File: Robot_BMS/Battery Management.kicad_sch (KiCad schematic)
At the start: 33 parts, among them IC2 BQ76922RSNR, Q4 SIS413DN-T1-GE3, Q5 2N7002, Q6 SIS413DN-T1-GE3

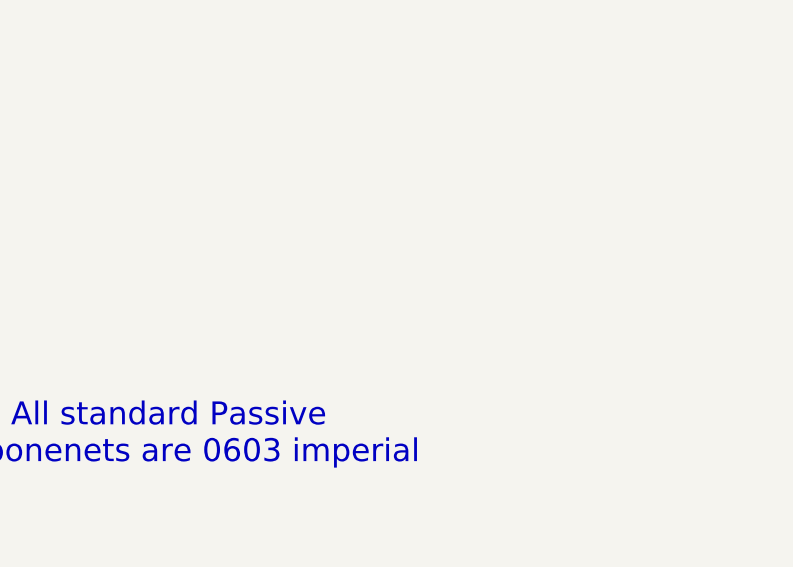
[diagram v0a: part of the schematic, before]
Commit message: adding qwik connectors replacing old jst ph 6 pin ones
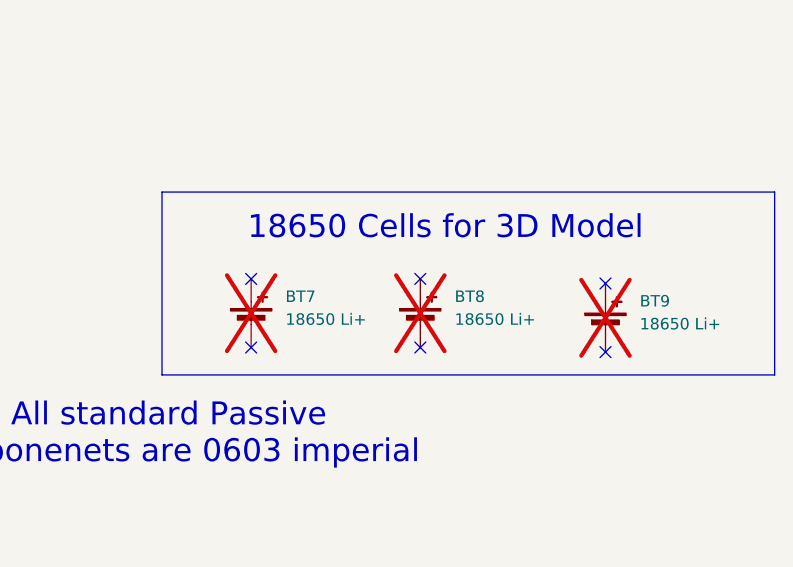
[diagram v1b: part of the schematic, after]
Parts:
- added BT7, BT8, BT9: 18650 Li+, RobotBMS:18650 Battery, symbol Device:Battery_Cell
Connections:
- no-connect marks 6 -> 12
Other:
- note added: "18650 Cells for 3D Model"
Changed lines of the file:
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@@
 	)
 	(no_connect
+		(at 226.06 162.814)
+	)
+	(no_connect
+		(at 265.43 155.702)
+	)
+	(no_connect
 		(at 130.048 122.936)
 	)
 	(no_connect
+		(at 265.43 163.322)
+	)
+	(no_connect
 		(at 127.508 122.936)
 	)
 	(no_connect
+		(at 244.856 162.814)
+	)
+	(no_connect
+		(at 226.06 155.194)
+	)
+	(no_connect
+		(at 244.856 155.194)
+	)
+	(no_connect
 		(at 145.288 94.996)
 	)
@@
 		)
 	)
+	(rectangle
+		(start 216.154 145.542)
+		(end 284.226 165.862)
+		(stroke
+			(width 0)
+			(type default)
+		)
+		(fill
+			(type none)
+		)
+	)
 	(text "Wires highlighted\nto avoid confusion\ndue to crossovers"
 		(exclude_from_sim no)
@@
 		)
 	)
+	(text "18650 Cells for 3D Model\n"
+		(exclude_from_sim no)
+		(at 247.65 149.606 0)
+		(effects
+			(font
+				(size 2.54 2.54)
+			)
+		)
+	)
 	(text "10A Resettable fuse\n\n"
 		(exclude_from_sim no)
@@
 	)
 	(symbol
+		(lib_id "Device:Battery_Cell")
+		(at 226.06 160.274 0)
+		(unit 1)
+		(exclude_from_sim no)
+		(in_bom no)
+		(on_board yes)
+		(dnp yes)
+		(fields_autoplaced yes)
+		(property "Reference" "BT7"
+			(at 229.87 157.1624 0)
+			(effects
+				(font
+					(size 1.27 1.27)
+				)
+				(justify left)
+			)
+		)
+		(property "Value" "18650 Li+"
+			(at 229.87 159.7024 0)
+			(effects
+				(font
+					(size 1.27 1.27)
+				)
+				(justify left)
+			)
+		)
+		(property "Footprint" "RobotBMS:18650 Battery"
+			(at 226.06 158.75 90)
+			(effects
+				(font
+					(size 1.27 1.27)
+				)
+				(hide yes)
+			)
+		)
+		(property "Datasheet" "~"
+			(at 226.06 158.75 90)
+			(effects
+				(font
+					(size 1.27 1.27)
+				)
+				(hide yes)
+			)
+		)
+		(property "Description" "Single-cell battery"
+			(at 226.06 160.274 0)
+			(effects
+				(font
+					(size 1.27 1.27)
+				)
+				(hide yes)
+			)
+		)
+		(pin "1"
+		)
+		(pin "2"
+		)
+		(instances
+			(project ""
+				(path "/72551b1c-3d40-4199-8911-e5b015f4abec/26a1c9c5-a214-45fb-a345-5a76cfe84f03"
+					(reference "BT7")
+					(unit 1)
+				)
+			)
+		)
+	)
+	(symbol
 		(lib_name "BK-18650-CLIP_1")
 		(lib_id "BK-18650-Clip:BK-18650-CLIP")
@@
 	)
 	(symbol
+		(lib_id "Device:Battery_Cell")
+		(at 265.43 160.782 0)
+		(unit 1)
+		(exclude_from_sim no)
+		(in_bom no)
+		(on_board yes)
+		(dnp yes)
+		(fields_autoplaced yes)
+		(property "Reference" "BT9"
+			(at 269.24 157.6704 0)
+			(effects
+				(font
+					(size 1.27 1.27)
+				)
+				(justify left)
+			)
+		)
+		(property "Value" "18650 Li+"
+			(at 269.24 160.2104 0)
+			(effects
+				(font
+					(size 1.27 1.27)
+				)
+				(justify left)
+			)
+		)
+		(property "Footprint" "RobotBMS:18650 Battery"
+			(at 265.43 159.258 90)
+			(effects
+				(font
+					(size 1.27 1.27)
+				)
+				(hide yes)
+			)
+		)
+		(property "Datasheet" "~"
+			(at 265.43 159.258 90)
+			(effects
+				(font
+					(size 1.27 1.27)
+				)
+				(hide yes)
+			)
+		)
+		(property "Description" "Single-cell battery"
+			(at 265.43 160.782 0)
+			(effects
+				(font
+					(size 1.27 1.27)
+				)
+				(hide yes)
+			)
+		)
+		(pin "1"
+		)
+		(pin "2"
+		)
+		(instances
+			(project "Robot_BMS"
+				(path "/72551b1c-3d40-4199-8911-e5b015f4abec/26a1c9c5-a214-45fb-a345-5a76cfe84f03"
+					(reference "BT9")
+					(unit 1)
+				)
+			)
+		)
+	)
+	(symbol
 		(lib_name "BK-18650-CLIP_1")
 		(lib_id "BK-18650-Clip:BK-18650-CLIP")
@@
 					(unit 1)
 				)
+			)
+		)
+	)
+	(symbol
+		(lib_id "Device:Battery_Cell")
+		(at 244.856 160.274 0)
+		(unit 1)
+		(exclude_from_sim no)
+		(in_bom no)
+		(on_board yes)
+		(dnp yes)
+		(fields_autoplaced yes)
+		(property "Reference" "BT8"
+			(at 248.666 157.1624 0)
+			(effects
+				(font
+					(size 1.27 1.27)
+				)
+				(justify left)
+			)
+		)
+		(property "Value" "18650 Li+"
+			(at 248.666 159.7024 0)
+			(effects
+				(font
+					(size 1.27 1.27)
+				)
+				(justify left)
+			)
+		)
+		(property "Footprint" "RobotBMS:18650 Battery"
+			(at 244.856 158.75 90)
+			(effects
+				(font
+					(size 1.27 1.27)
+				)
+				(hide yes)
+			)
+		)
+		(property "Datasheet" "~"
+			(at 244.856 158.75 90)
+			(effects
+				(font
+					(size 1.27 1.27)
+				)
+				(hide yes)
+			)
+		)
+		(property "Description" "Single-cell battery"
+			(at 244.856 160.274 0)
+			(effects
+				(font
+					(size 1.27 1.27)
+				)
+				(hide yes)
+			)
+		)
+		(pin "1"
+		)
+		(pin "2"
+		)
+		(instances
+			(project "Robot_BMS"
+				(path "/72551b1c-3d40-4199-8911-e5b015f4abec/26a1c9c5-a214-45fb-a345-5a76cfe84f03"
+					(reference "BT8")
+					(unit 1)
+				)

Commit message: creation of seperate 4 layer pcb for individual technical report
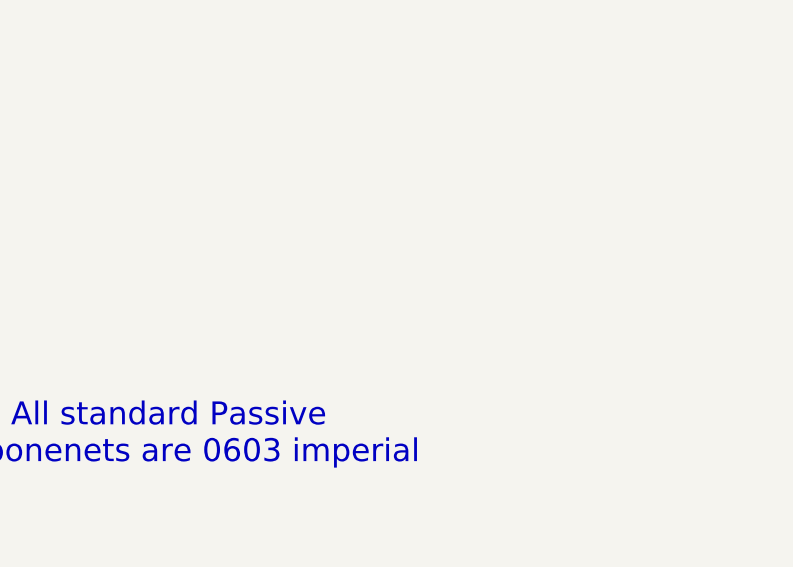
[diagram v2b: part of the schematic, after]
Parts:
- removed BT7, BT8, BT9: 18650 Li+, RobotBMS:18650 Battery, symbol Device:Battery_Cell
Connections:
- no-connect marks 12 -> 6
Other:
- note removed: "18650 Cells for 3D Model"

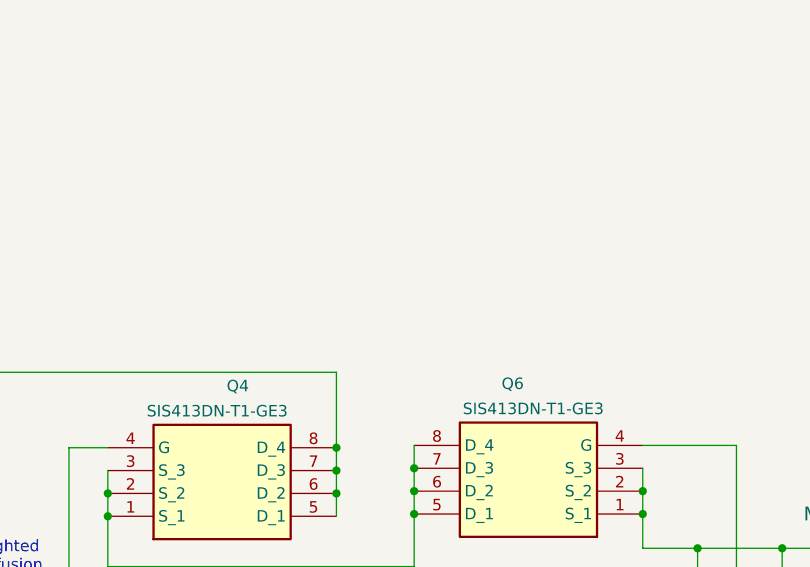
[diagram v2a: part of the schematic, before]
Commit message: PCB layout up to charging circuit
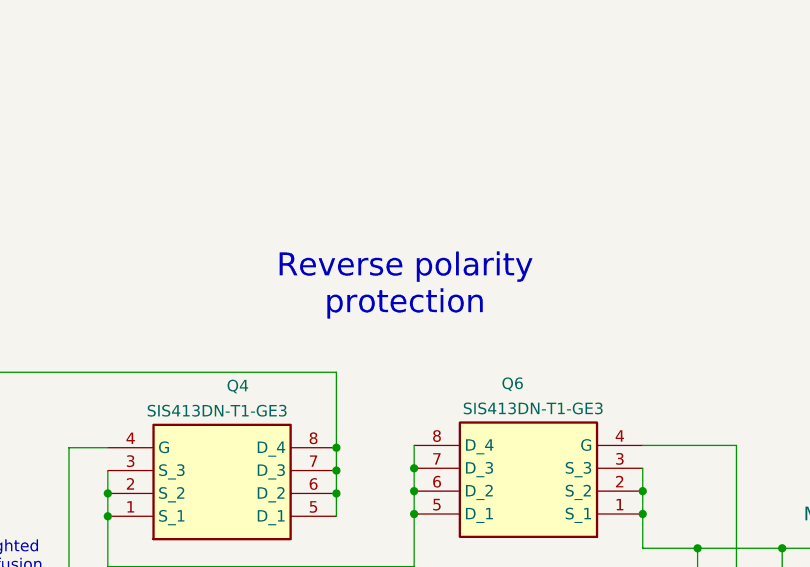
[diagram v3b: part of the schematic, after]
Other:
- note added: "Reverse polarity protection"
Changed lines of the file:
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@@
+		)
+	)
+	(text "Reverse polarity \nprotection"
+		(exclude_from_sim no)
+		(at 159.766 23.114 0)
+		(effects
+			(font
+				(size 2.54 2.54)
+			)
 		)
 	)

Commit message: halfway throgh battery management pcb layout
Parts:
- BT1, BT2, BT3, BT4, BT5, BT6: Manufacturer_Part_Number (none) -> BK-18650-CLIP
- renumbered R14 to R15, R15 to R16, R16 to R17, R17 to R18, R18 to R19, R19 to R20, R20 to R21, R21 to R22, R22 to R23, R23 to R24, R24 to R25, R25 to R26
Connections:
- net GND: no longer R21.1, R22.1
- new net TO_LOAD_GND: R21.1, R22.1
